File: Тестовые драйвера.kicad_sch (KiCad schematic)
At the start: 117 parts, among them J1 Conn_01x01, J10 Conn_01x01, J11 Conn_01x01, J12 Conn_01x01, J13 Conn_01x01, J14 Conn_01x03, J15 Conn_01x03, J16 Conn_01x03, J2 Conn_01x01, J3 Conn_01x01, J4 Conn_01x04, J5 Conn_01x04, J7 Conn_01x04, J8 Conn_01x01, J9 Conn_01x01, Q1 C2M0280120D, Q2 C2M0280120D, Q3 C2M0280120D, Q4 C2M0280120D, Q5 C2M0280120D, Q6 C2M0280120D

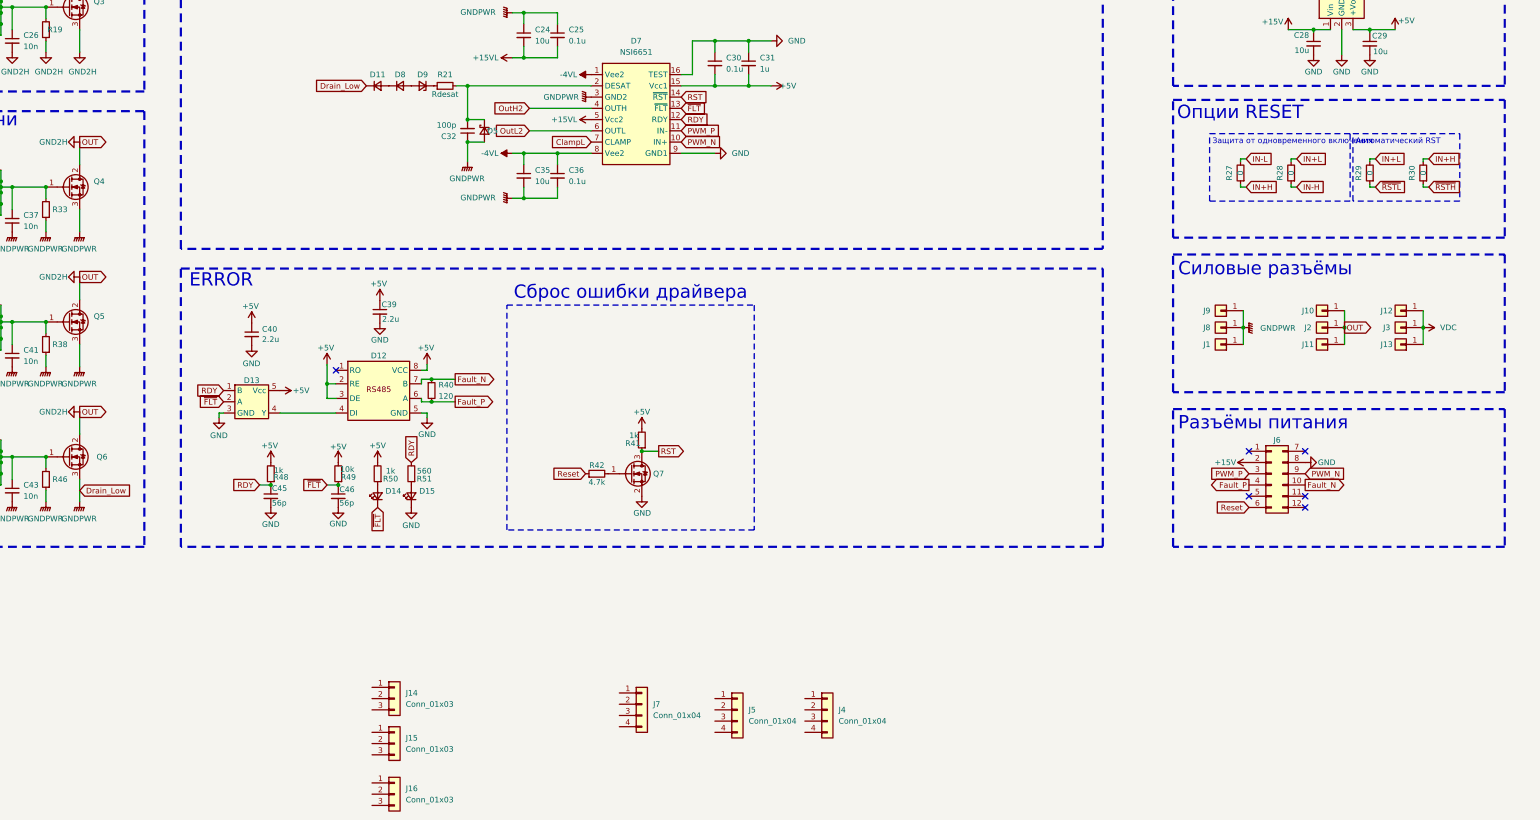
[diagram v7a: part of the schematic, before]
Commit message: VER1.0.2: развел нижнюю сторону
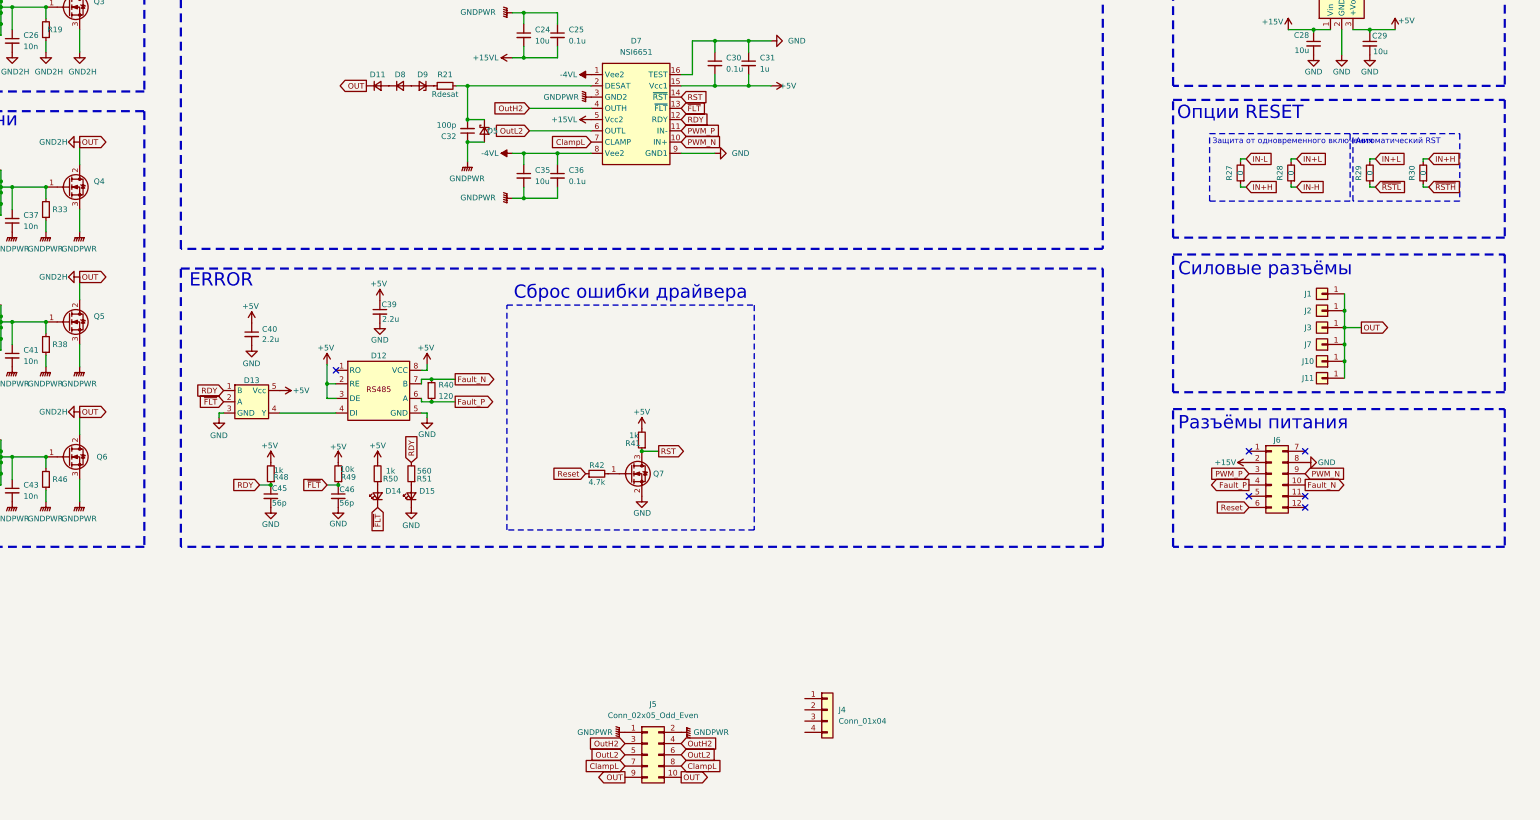
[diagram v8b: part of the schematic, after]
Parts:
- removed J12, J13, J8, J9: Conn_01x01, Bush_my:Bush_5x3, symbol Connector_Generic:Conn_01x01
- removed J14, J15, J16: Conn_01x03, Bush_my:247_border_my, symbol Connector_Generic:Conn_01x03
- removed J5, J7: Conn_01x04, Connector_PinSocket_2.54mm:PinSocket_1x04_P2.54mm_Vertical, symbol Connector_Generic:Conn_01x04
- added J5: Conn_02x05_Odd_Even, Connector_PinSocket_2.54mm:PinSocket_2x05_P2.54mm_Vertical, symbol Connector_Generic:Conn_02x05_Odd_Even
- added J7: Conn_01x01, Bush_my:Bush_5x3, symbol Connector_Generic:Conn_01x01
- J4: footprint Connector_PinSocket_2.54mm:PinSocket_1x04_P2.54mm_Vertical -> Connector_PinSocket_2.54mm:PinSocket_2x04_P2.54mm_Vertical
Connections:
- net ClampL: now also J5.7 (Pin_7), J5.8 (Pin_8)
- net GND2H: now also D11.1 (K), J1.1 (Pin_1), J3.1 (Pin_1), J5.10 (Pin_10), J5.9 (Pin_9), J7.1 (Pin_1)
- net GNDPWR: now also J5.1 (Pin_1), J5.2 (Pin_2); no longer D11.1 (K), J1.1 (Pin_1)
- net OutH2: now also J5.3 (Pin_3), J5.4 (Pin_4)
- net OutL2: now also J5.5 (Pin_5), J5.6 (Pin_6)
- net VDC: no longer J3.1 (Pin_1)
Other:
- moved on the sheet: J10, J11, J2
